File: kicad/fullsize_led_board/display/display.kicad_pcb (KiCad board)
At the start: 2 copper layers, 233.5 x 181.5 mm, 776 parts, among them J1 Anodes Header, J2 Cathodes Header, J3 Stabilizer Header (Top), J4 Stabilizer Header (Left)

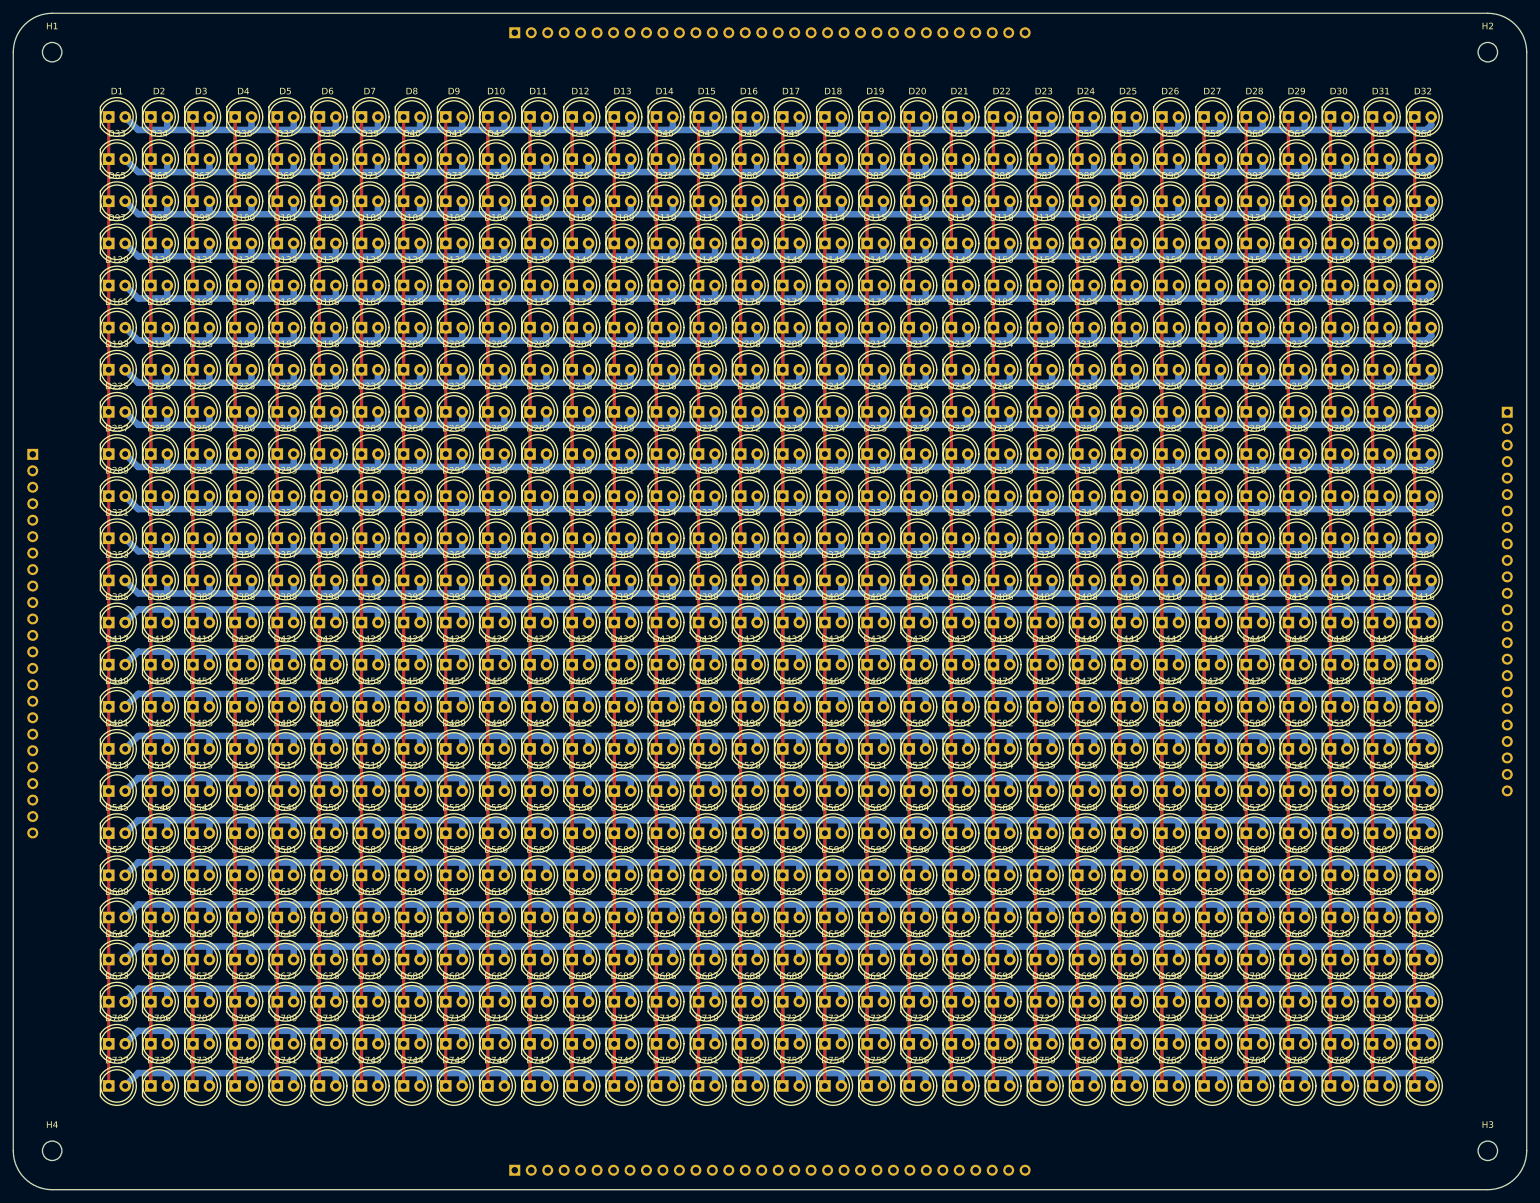
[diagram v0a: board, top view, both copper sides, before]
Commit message: fullsize led board: display pcb wired
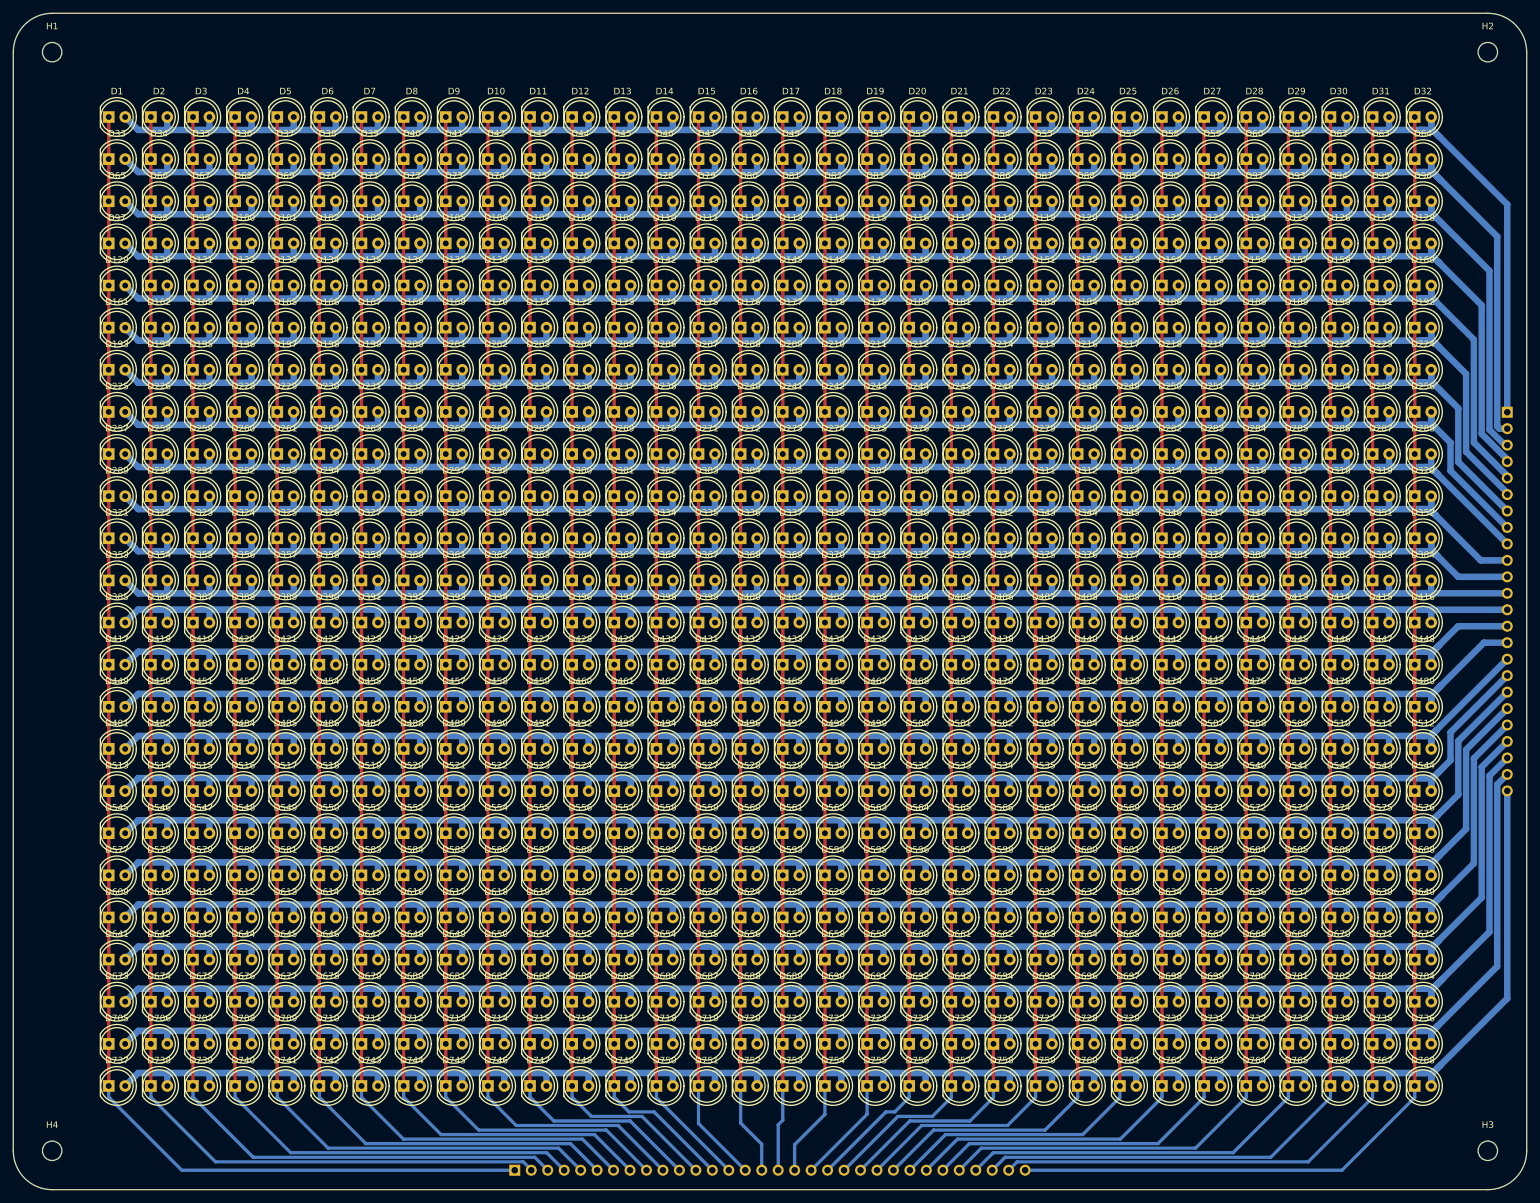
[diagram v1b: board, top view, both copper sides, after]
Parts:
- removed J3: Stabilizer Header (Top), Connector_PinHeader_2.54mm:PinHeader_1x32_P2.54mm_Vertical
- removed J4: Stabilizer Header (Left), Connector_PinHeader_2.54mm:PinHeader_1x24_P2.54mm_Vertical
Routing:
- net /Cathodes0: track 149.5 -> 218.5 mm
- net /Cathodes31: track 149.5 -> 216.0 mm
- net /Cathodes1: track 149.5 -> 214.6 mm
- net /Cathodes30: track 149.5 -> 212.1 mm
- net /Cathodes2: track 149.5 -> 210.6 mm
- net /Cathodes29: track 149.5 -> 208.1 mm
- net /Cathodes3: track 149.5 -> 206.7 mm
- net /Cathodes28: track 149.5 -> 204.2 mm
- net /Anodes23: track 266.8 -> 320.5 mm
- net /Cathodes4: track 149.5 -> 202.7 mm
- net /Anodes0: track 266.8 -> 319.6 mm
- net /Anodes1: track 266.8 -> 317.7 mm
- net /Cathodes27: track 149.5 -> 200.2 mm
- net /Anodes22: track 266.8 -> 316.8 mm
- net /Cathodes5: track 149.5 -> 198.7 mm
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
